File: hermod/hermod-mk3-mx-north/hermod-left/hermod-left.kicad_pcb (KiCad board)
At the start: 2 copper layers, 198.5 x 173.6 mm, 205 parts, among them J1 USB_C_Receptacle_USB2.0, J2 Conn_01x05, J3 USB_C_Receptacle_USB2.0, Q3 MMUN2133LT1G, U1 STM32G474CETx, U2 PRTR5V0U2X, U3 XC6206PxxxMR-Regulator_Linear, U4 CR2013-MI2120, U5 PRTR5V0U2X, U8 SN74AHCT1G125DBVR

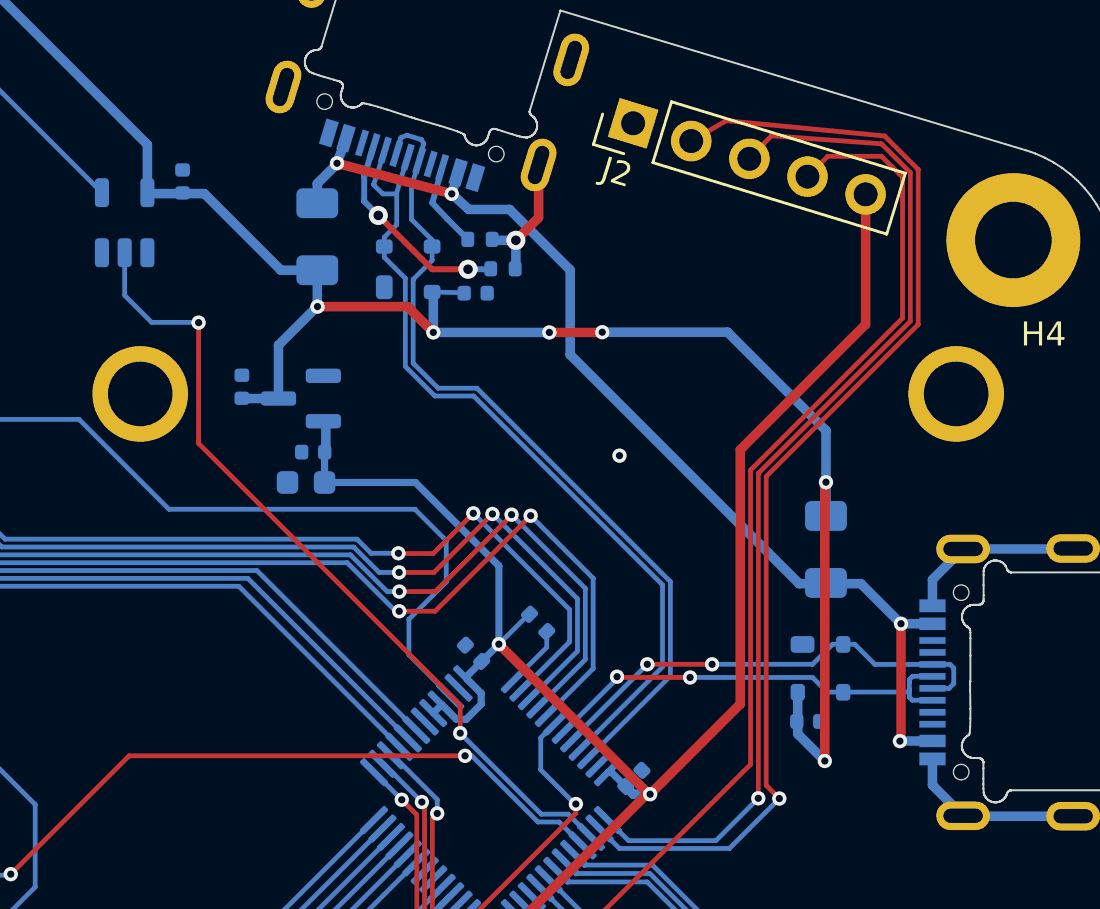
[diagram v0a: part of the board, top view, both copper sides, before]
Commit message: Switched to SRV05-4
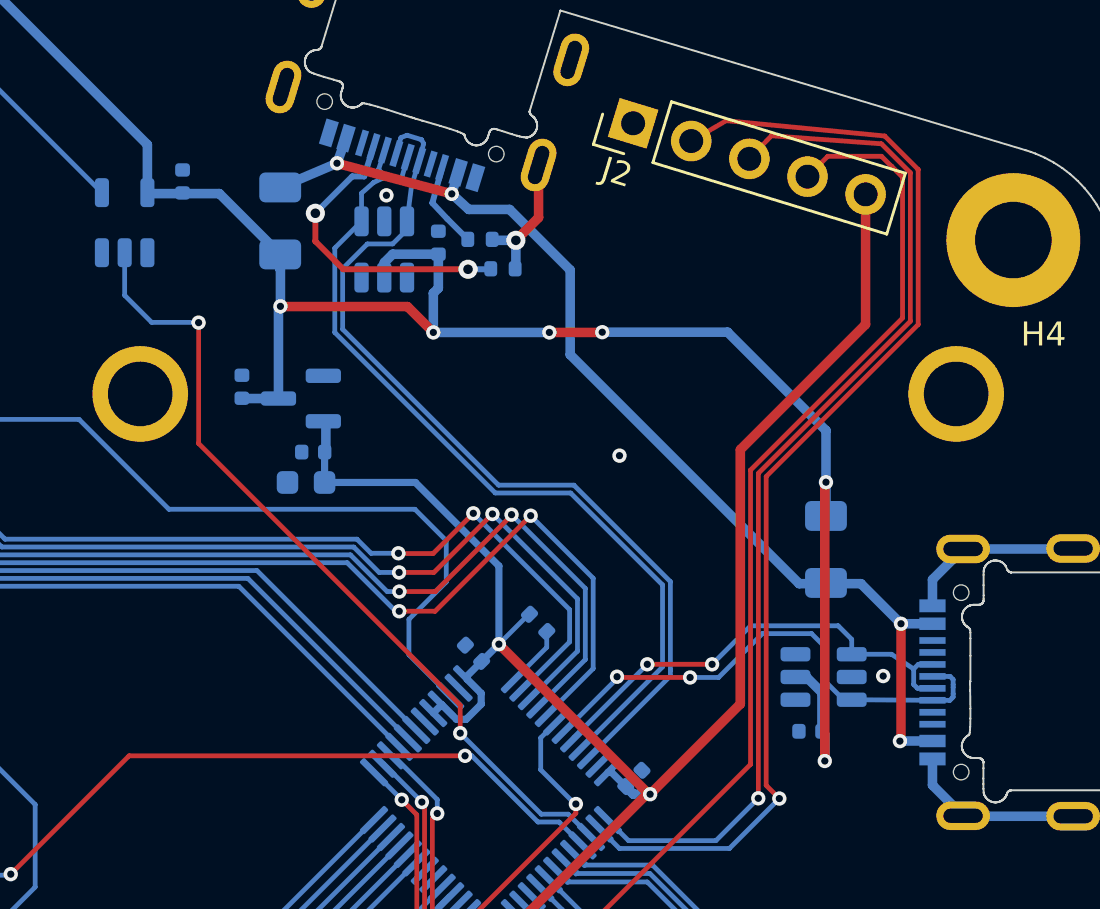
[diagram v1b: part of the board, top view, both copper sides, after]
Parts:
- removed U5: PRTR5V0U2X, Package_TO_SOT_SMD:SOT-143
- added U9: SRV05-4, PCM_marbastlib-various:SOT-23-6-routable, B.Cu at (274.4, 49.7)
- U2: value PRTR5V0U2X -> SRV05-4; footprint Package_TO_SOT_SMD:SOT-143 -> PCM_marbastlib-various:SOT-23-6-routable
- moved U2 24.3 mm to (292.8, 67.5), turned to 180 degrees
- moved C108 2.62 mm to (276.6, 49.4), turned to 90 degrees
- moved F1 1.68 mm to (270.0, 48.5)
- moved C56 0.42 mm to (292.2, 69.8), turned to 180 degrees
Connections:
- U2 pad 1: GND -> SplitSerial-RX
- U2 pad 2: D- -> GND
- U2 pad 3: D+ -> SplitSerial-TX
- U2 pad 4: +5V -> unconnected-(U2-IO3-Pad4)
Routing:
- net Net-(J1-CC1): track 8.73 -> 12.9 mm
- net +5V: track 1106.4 -> 1110.5 mm
- net SplitSerial-TX: track 18.0 -> 21.4 mm
- net D+: track 34.8 -> 38.1 mm
- net D-: track 34.7 -> 36.6 mm
- net VBUS: track 44.9 -> 45.5 mm
- net GND: vias 56 -> 58
